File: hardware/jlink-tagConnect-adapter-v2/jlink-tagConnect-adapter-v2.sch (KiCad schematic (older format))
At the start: 15 parts, among them J1 Conn_02x10_Odd_Even, J2 Conn_02x05_Odd_Even, J3 Conn_02x05_Odd_Even, J4 Conn_01x10, J5 Conn_01x03

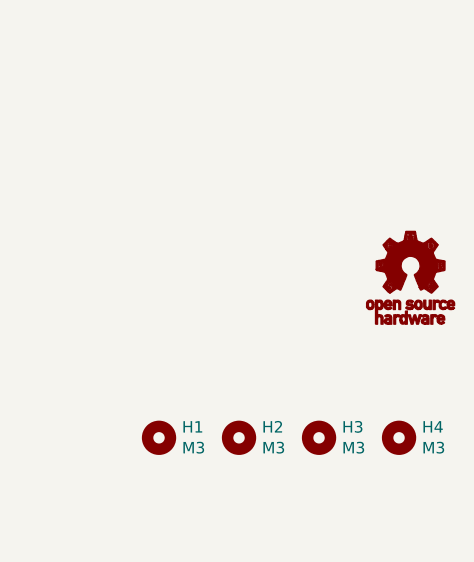
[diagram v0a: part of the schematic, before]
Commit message: Changed OSHW logo
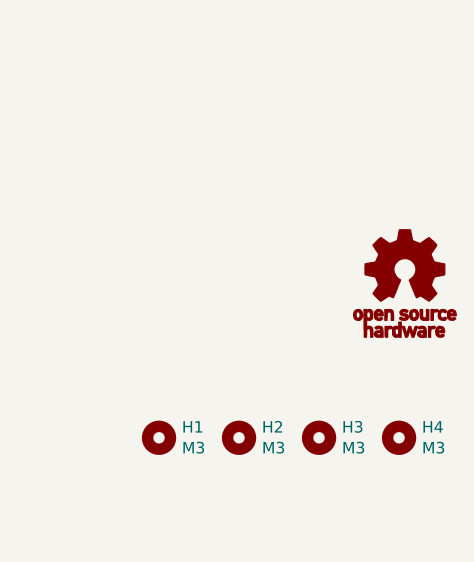
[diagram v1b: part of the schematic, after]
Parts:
- removed G1: Symbol_OSHW-EEVBLOG_SPFMDBC_10mm, symbol BrechtVE_Aesthetics:Symbol_OSHW-EEVBLOG_SPFMDBC_10mm
- added G1: Symbol_OSHW-Logo_11.4x12mm, symbol BrechtVE_Aesthetics:Symbol_OSHW-Logo_11.4x12mm
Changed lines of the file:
@@
 $EndDescr
 $Comp
-L BrechtVE_Aesthetics:Symbol_OSHW-EEVBLOG_SPFMDBC_10mm G1
-U 1 1 5DDC2639
-P 11000 6350
-F 0 "G1" H 11000 6175 60  0001 C CNN
-F 1 "Symbol_OSHW-EEVBLOG_SPFMDBC_10mm" H 11000 6525 60  0001 C CNN
-F 2 "" H 11000 6350 50  0001 C CNN
-F 3 "" H 11000 6350 50  0001 C CNN
-	1    11000 6350
-	1    0    0    -1
-$EndComp
-$Comp
 L Connector_Generic:Conn_02x10_Odd_Even J1
 U 1 1 5DDC45BE
@@
 Text Label 2400 5600 2    50   ~ 0
 VTREF
+$Comp
+L BrechtVE_Aesthetics:Symbol_OSHW-Logo_11.4x12mm G1
+U 1 1 5DDCA46F
+P 10975 6375
+F 0 "G1" H 10975 6170 60  0001 C CNN
+F 1 "Symbol_OSHW-Logo_11.4x12mm" H 10975 6580 60  0001 C CNN
+F 2 "" H 10975 6375 50  0001 C CNN
+F 3 "" H 10975 6375 50  0001 C CNN
+	1    10975 6375
+	1    0    0    -1
+$EndComp
 $EndSCHEMATC

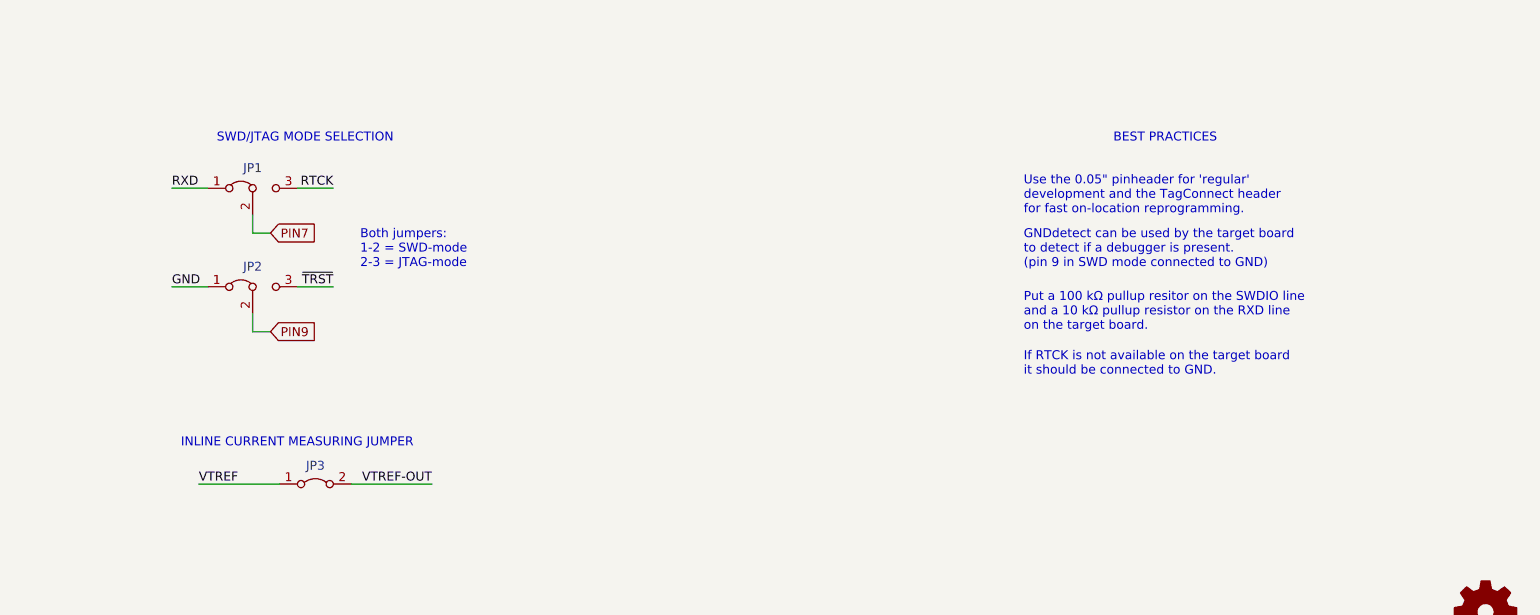
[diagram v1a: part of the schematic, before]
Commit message: Updated with new debug header symbols
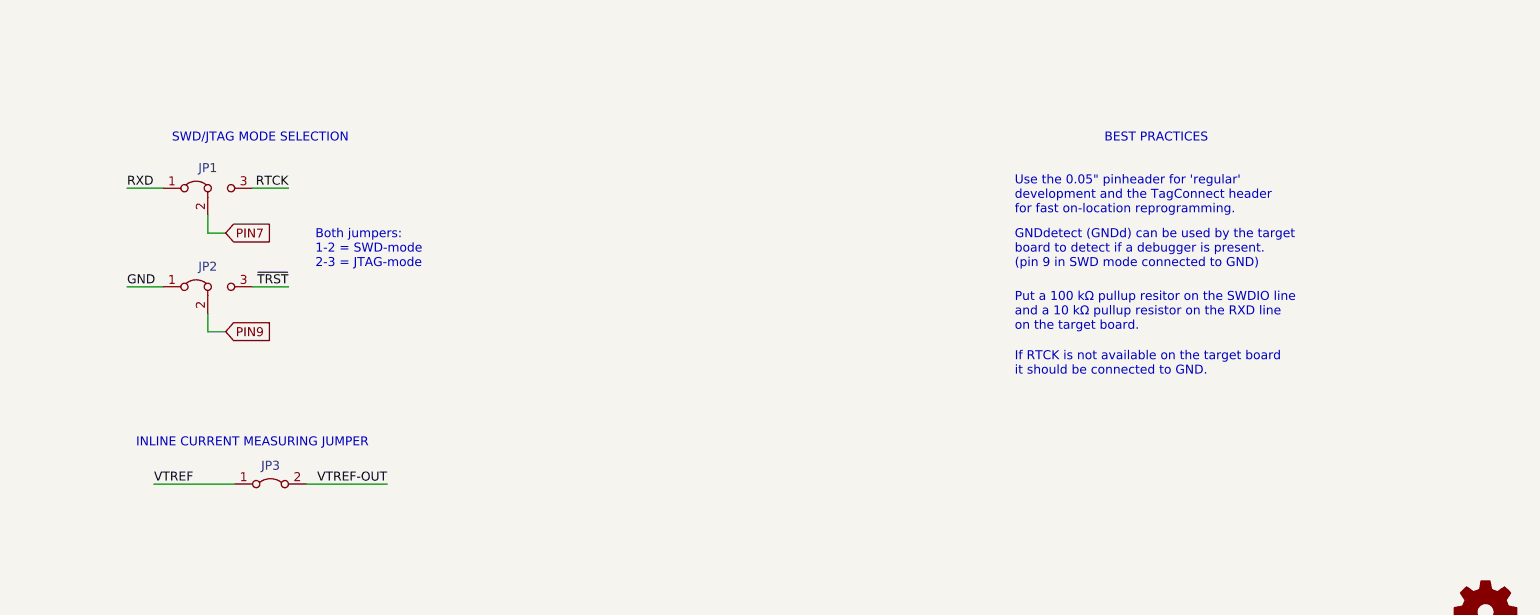
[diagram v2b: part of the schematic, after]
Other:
- note added: "GNDdetect (GNDd) can be used by the target\nboard to detect if a debugger is present.\n(pin 9 in SWD mode connected to GND)"
- note removed: "GNDdetect can be used by the target board\nto detect if a debugger is present.\n(pin 9 in SWD mode connected to GND)"
- moved on the sheet: JP1, JP2, JP3
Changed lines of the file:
@@
 Text Notes 3650 1150 0    50   ~ 0
 SWD/JTAG OUTPUT HEADERS
-Text Notes 3900 3700 0    50   ~ 0
+Text Notes 3650 3700 0    50   ~ 0
 SWD/JTAG MODE SELECTION
 $Comp
 L Jumper:Jumper_3_Bridged12 JP1
 U 1 1 5DE49560
-P 4100 3950
-F 0 "JP1" H 4100 4063 50  0000 C CNN
-F 1 "Jumper_3_Bridged12" H 4100 4063 50  0001 C CNN
-F 2 "" H 4100 3950 50  0001 C CNN
-F 3 "~" H 4100 3950 50  0001 C CNN
-	1    4100 3950
+P 3850 3950
+F 0 "JP1" H 3850 4063 50  0000 C CNN
+F 1 "Jumper_3_Bridged12" H 3850 4063 50  0001 C CNN
+F 2 "" H 3850 3950 50  0001 C CNN
+F 3 "~" H 3850 3950 50  0001 C CNN
+	1    3850 3950
 	1    0    0    -1
 $EndComp
@@
 L Jumper:Jumper_3_Bridged12 JP2
 U 1 1 5DE49D82
-P 4100 4500
-F 0 "JP2" H 4100 4613 50  0000 C CNN
-F 1 "Jumper_3_Bridged12" H 4100 4613 50  0001 C CNN
-F 2 "" H 4100 4500 50  0001 C CNN
-F 3 "~" H 4100 4500 50  0001 C CNN
-	1    4100 4500
-	1    0    0    -1
-$EndComp
-Text GLabel 4200 4200 2    50   Input ~ 0
+P 3850 4500
+F 0 "JP2" H 3850 4613 50  0000 C CNN
+F 1 "Jumper_3_Bridged12" H 3850 4613 50  0001 C CNN
+F 2 "" H 3850 4500 50  0001 C CNN
+F 3 "~" H 3850 4500 50  0001 C CNN
+	1    3850 4500
+	1    0    0    -1
+$EndComp
+Text GLabel 3950 4200 2    50   Input ~ 0
 PIN7
-Text GLabel 4200 4750 2    50   Input ~ 0
+Text GLabel 3950 4750 2    50   Input ~ 0
 PIN9
 Wire Wire Line
-	4100 4100 4100 4200
-Wire Wire Line
-	4100 4200 4200 4200
-Wire Wire Line
-	4100 4650 4100 4750
-Wire Wire Line
-	4100 4750 4200 4750
-Wire Wire Line
-	3850 3950 3650 3950
-Text Label 3650 3950 0    50   ~ 0
+	3850 4100 3850 4200
+Wire Wire Line
+	3850 4200 3950 4200
+Wire Wire Line
+	3850 4650 3850 4750
+Wire Wire Line
+	3850 4750 3950 4750
+Wire Wire Line
+	3600 3950 3400 3950
+Text Label 3400 3950 0    50   ~ 0
 RXD
-Text Notes 4700 4400 0    50   ~ 0
+Text Notes 4450 4400 0    50   ~ 0
 Both jumpers:\n1-2 = SWD-mode\n2-3 = JTAG-mode
 Wire Wire Line
-	3850 4500 3650 4500
-Text Label 3650 4500 0    50   ~ 0
+	3600 4500 3400 4500
+Text Label 3400 4500 0    50   ~ 0
 GND
-Text Notes 8400 4400 0    50   ~ 0
-GNDdetect can be used by the target board\nto detect if a debugger is present.\n(pin 9 in SWD mode connected to GND)
-Wire Wire Line
-	4350 3950 4550 3950
-Text Label 4550 3950 2    50   ~ 0
+Wire Wire Line
+	4100 3950 4300 3950
+Text Label 4300 3950 2    50   ~ 0
 RTCK
 Wire Wire Line
-	4350 4500 4550 4500
-Text Label 4550 4500 2    50   ~ 0
+	4100 4500 4300 4500
+Text Label 4300 4500 2    50   ~ 0
 ~TRST
 Text Notes 5950 1150 0    50   ~ 0
@@
 Text Label 6100 2450 0    50   ~ 0
 5V-Supply
-Text Notes 8400 5000 0    50   ~ 0
-If RTCK is not available on the target board\nit should be connected to GND.
-Text Notes 8400 4750 0    50   ~ 0
-Put a 100 kΩ pullup resitor on the SWDIO line\nand a 10 kΩ pullup resistor on the RXD line \non the target board.
-Text Notes 8900 3700 0    50   ~ 0
-BEST PRACTICES
-Text Notes 8400 4100 0    50   ~ 0
-Use the 0.05" pinheader for 'regular'\ndevelopment and the TagConnect header\nfor fast on-location reprogramming.
 $Comp
 L Mechanical:MountingHole H1
@@
 L Jumper:Jumper_2_Bridged JP3
 U 1 1 5DF28FF9
-P 4450 5600
-F 0 "JP3" H 4450 5703 50  0000 C CNN
-F 1 "Jumper_2_Bridged" H 4450 5704 50  0001 C CNN
-F 2 "" H 4450 5600 50  0001 C CNN
-F 3 "~" H 4450 5600 50  0001 C CNN
-	1    4450 5600
-	1    0    0    -1
-$EndComp
-Text Notes 3700 5400 0    50   ~ 0
+P 4200 5600
+F 0 "JP3" H 4200 5703 50  0000 C CNN
+F 1 "Jumper_2_Bridged" H 4200 5704 50  0001 C CNN
+F 2 "" H 4200 5600 50  0001 C CNN
+F 3 "~" H 4200 5600 50  0001 C CNN
+	1    4200 5600
+	1    0    0    -1
+$EndComp
+Text Notes 3450 5400 0    50   ~ 0
 INLINE CURRENT MEASURING JUMPER
 Wire Wire Line
-	4650 5600 5100 5600
-Text Label 5100 5600 2    50   ~ 0
+	4400 5600 4850 5600
+Text Label 4850 5600 2    50   ~ 0
 VTREF-OUT
 $Comp
@@
 VTREF-OUT
 Wire Wire Line
-	4250 5600 3800 5600
-Text Label 3800 5600 0    50   ~ 0
+	4000 5600 3550 5600
+Text Label 3550 5600 0    50   ~ 0
 VTREF
 Text Notes 1350 3700 0    50   ~ 0
@@
 	1    0    0    -1
 $EndComp
+Text Notes 8350 4100 0    50   ~ 0
+Use the 0.05" pinheader for 'regular'\ndevelopment and the TagConnect header\nfor fast on-location reprogramming.
+Text Notes 8850 3700 0    50   ~ 0
+BEST PRACTICES
+Text Notes 8350 4750 0    50   ~ 0
+Put a 100 kΩ pullup resitor on the SWDIO line\nand a 10 kΩ pullup resistor on the RXD line \non the target board.
+Text Notes 8350 5000 0    50   ~ 0
+If RTCK is not available on the target board\nit should be connected to GND.
+Text Notes 8350 4400 0    50   ~ 0
+GNDdetect (GNDd) can be used by the target\nboard to detect if a debugger is present.\n(pin 9 in SWD mode connected to GND)
 $EndSCHEMATC

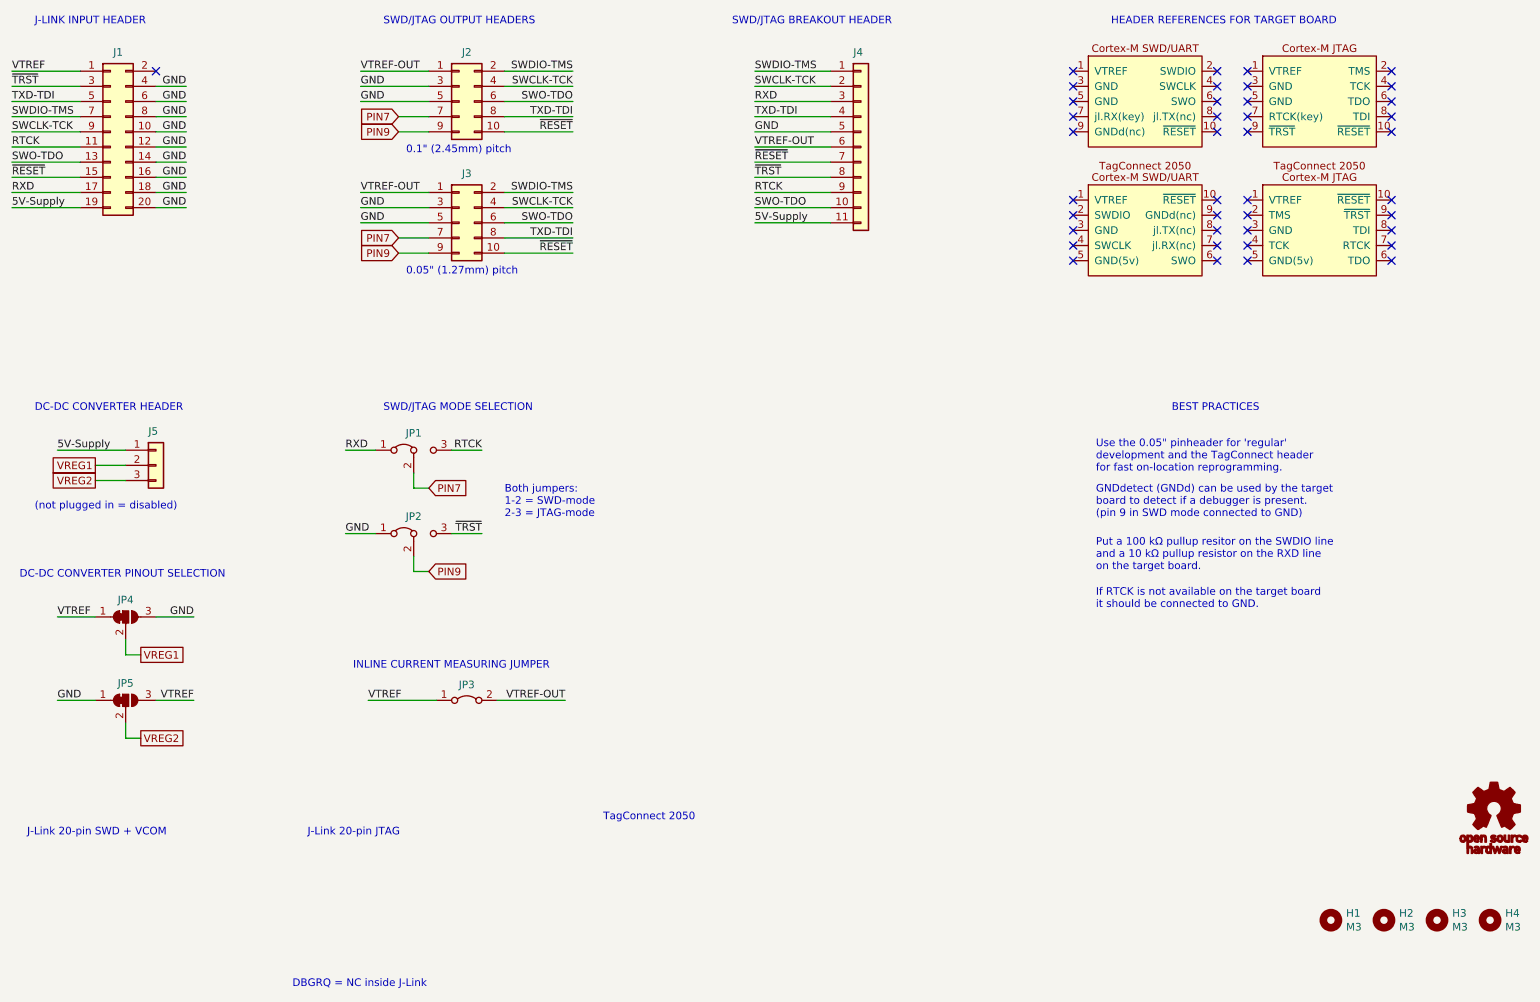
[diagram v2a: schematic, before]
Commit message: Updated schematic with new title
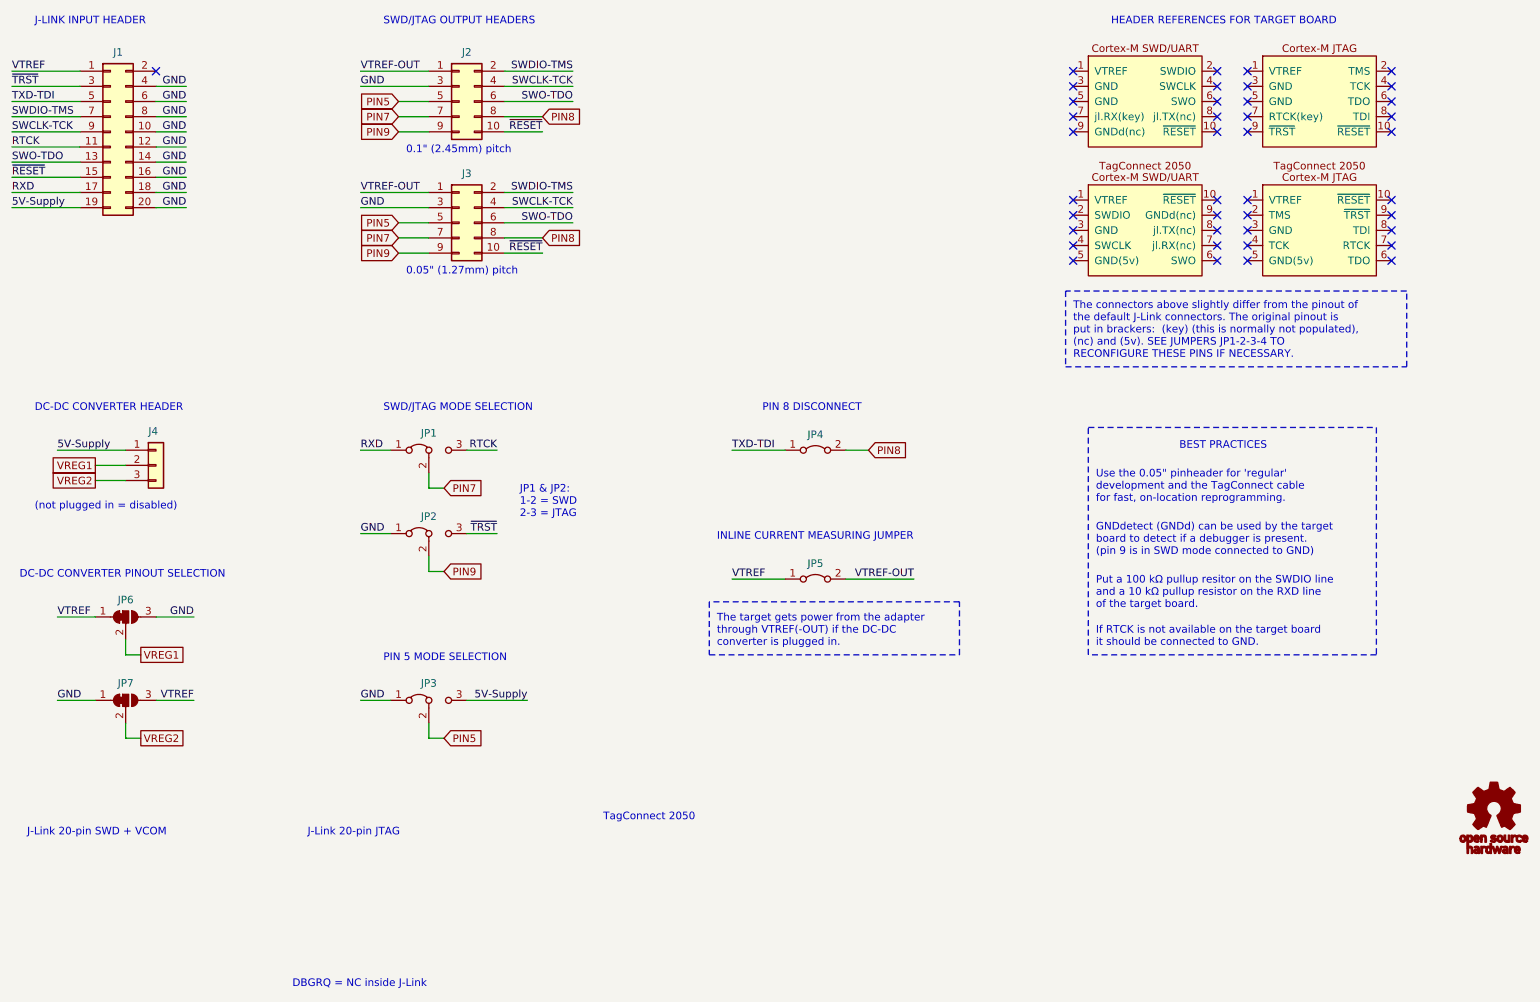
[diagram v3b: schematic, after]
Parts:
- removed H1, H2, H3, H4: M3, symbol Mechanical:MountingHole
- removed J4: Conn_01x10, symbol Connector_Generic:Conn_01x11
- added JP3: Jumper_3_Bridged12, Connector_PinHeader_2.54mm:PinHeader_1x03_P2.54mm_Vertical, symbol Jumper:Jumper_3_Bridged12
- added JP4: Jumper_2_Bridged, Connector_PinHeader_2.54mm:PinHeader_1x02_P2.54mm_Vertical, symbol Jumper:Jumper_2_Bridged
- G1: footprint (none) -> BrechtVE_Aesthetics:OSHW-Logo_5.7x6mm_SolderMask
- J1: footprint (none) -> Connector_PinSocket_2.54mm:PinSocket_2x10_P2.54mm_Horizontal
- J2: footprint (none) -> Connector_IDC:IDC-Header_2x05_P2.54mm_Vertical
- J3: footprint (none) -> Connector_PinHeader_1.27mm:PinHeader_2x05_P1.27mm_Vertical_SMD
- J4: renamed from J5; footprint (none) -> Connector_PinSocket_2.54mm:PinSocket_1x03_P2.54mm_Vertical
- JP1, JP2: footprint (none) -> Connector_PinHeader_2.54mm:PinHeader_1x03_P2.54mm_Vertical
- JP5: renamed from JP3; footprint (none) -> Connector_PinHeader_2.54mm:PinHeader_1x02_P2.54mm_Vertical
- JP6: renamed from JP4; footprint (none) -> Jumper:SolderJumper-3_P1.3mm_Bridged12_Pad1.0x1.5mm_NumberLabels
- JP7: renamed from JP5; footprint (none) -> Jumper:SolderJumper-3_P1.3mm_Bridged12_Pad1.0x1.5mm_NumberLabels
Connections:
- net 5V-Supply: now also JP3.3 (B)
- net GND: now also JP3.1 (A); no longer J2.5 (Pin_5), J3.5 (Pin_5)
- net TXD-TDI: now also JP4.1 (A); no longer J2.8 (Pin_8), J3.8 (Pin_8)
- new net PIN5: J2.5 (Pin_5), J3.5 (Pin_5), JP3.2 (C)
- new net PIN8: J2.8 (Pin_8), J3.8 (Pin_8), JP4.2 (B)
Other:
- note added: "GNDdetect (GNDd) can be used by the target\nboard to detect if a debugger is present.\n(pin 9 is in SWD mode connected to GND)"
- note added: "JP1 & JP2:\n1-2 = SWD\n2-3 = JTAG"
- note added: "PIN 5 MODE SELECTION"
- note added: "PIN 8 DISCONNECT"
- note added: "Put a 100 kΩ pullup resitor on the SWDIO line\nand a 10 kΩ pullup resistor on the RXD line \nof the target board."
- note added: "The connectors above slightly differ from the pinout of\nthe default J-Link connectors. The original pinout is\nput in brackers: (key) (this is normally not populated),\n(nc) and (5v). SEE JUMPERS JP1-2-3-4 TO\nRECONFIGURE THESE PINS IF NECESSARY."
- note added: "The target gets power from the adapter\nthrough VTREF(-OUT) if the DC-DC \nconverter is plugged in."
- note added: "Use the 0.05" pinheader for 'regular'\ndevelopment and the TagConnect cable\nfor fast, on-location reprogramming."
- note removed: "Both jumpers:\n1-2 = SWD-mode\n2-3 = JTAG-mode"
- note removed: "GNDdetect (GNDd) can be used by the target\nboard to detect if a debugger is present.\n(pin 9 in SWD mode connected to GND)"
- note removed: "Put a 100 kΩ pullup resitor on the SWDIO line\nand a 10 kΩ pullup resistor on the RXD line \non the target board."
- note removed: "SWD/JTAG BREAKOUT HEADER"
- note removed: "Use the 0.05" pinheader for 'regular'\ndevelopment and the TagConnect header\nfor fast on-location reprogramming."
- moved on the sheet: JP1, JP2, JP5
